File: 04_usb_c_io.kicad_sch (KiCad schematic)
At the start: 38 parts, among them J11 USB-C downstream 1, J12 USB-C downstream 2, U21 TPS25810 Type-C DFP port 1, U22 HD3SS6126 USB3 orientation mu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, U23 TPD4EUSB30 TX ESD, U24 TPD4EUSB30 RX ESD, U25 TPD4EUSB30 USB2/CC ESD, U31 TPS25810 Type-C DFP port 2, U32 HD3SS6126 USB3 orientation mu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, U33 TPD4EUSB30 TX ESD, U34 TPD4EUSB30 RX ESD, U35 TPD4EUSB30 USB2/CC ESD

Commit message: Publish the current Ducktop2 design
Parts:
- removed C70: 10u TPS25810 IN, Capacitor_SMD:C_1206_3216Metric, symbol Device:C
- removed C71: 100n TPS25810 IN, Capacitor_SMD:C_0603_1608Metric, symbol Device:C
- removed C72: 100n AUX, Capacitor_SMD:C_0603_1608Metric, symbol Device:C
- removed C73: 100n mux VDD, Capacitor_SMD:C_0603_1608Metric, symbol Device:C
- removed R92: 10k UFP pull-up, Resistor_SMD:R_0603_1608Metric, symbol Device:R
- removed R93: 10k LD_DET pull-up, Resistor_SMD:R_0603_1608Metric, symbol Device:R
- removed R94: 100k REF, Resistor_SMD:R_0603_1608Metric, symbol Device:R
- removed U24: TPD4EUSB30 RX ESD, Package_SON:USON-10_2.5x1.0mm_P0.5mm, symbol Power_Protection:TPD4EUSB30
- removed U33: TPD4EUSB30 TX ESD, Package_SON:USON-10_2.5x1.0mm_P0.5mm, symbol Power_Protection:TPD4EUSB30
- added C98: 150u 10V TPS25810 input reservoir, Capacitor_Tantalum_SMD:CP_EIA-7343-31_Kemet-D, symbol Device:C_Polarized
- added C99: 10n mux high-frequency bypass, Capacitor_SMD:C_0603_1608Metric, symbol Device:C
- added D210, D211, D212, D213, D214, D215, D216, D217, D230, D231, D232, D233, D234, D235, D236, D237: TPD1E0B04DPL USB3 ESD, Diode_SMD:D_0201_0603Metric, symbol Device:D_TVS
- added R70: 20.0k 1% TPS2553 ILIM 1.3A nominal, Resistor_SMD:R_0603_1608Metric, symbol Device:R
- added R71: 4.99k 1% POL pull-up, Resistor_SMD:R_0603_1608Metric, symbol Device:R
- added R74: 100k 1% <=100ppm REF, Resistor_SMD:R_0603_1608Metric, symbol Device:R
- added U20: TPS2553DDBVR USB-C port 1 1.3A branch switch, Package_TO_SOT_SMD:SOT-23-6, symbol TPS2553D:TPS2553D
- added U30: TPS2553DDBVR USB-C port 2 1.3A branch switch, Package_TO_SOT_SMD:SOT-23-6, symbol TPS2553D:TPS2553D
- C70: renamed from C74; value 100n mux VDD -> 100n TPS2553 input bypass
- C71: renamed from C75; value 10u port VBUS -> 100n TPS25810 IN; footprint Capacitor_SMD:C_1206_3216Metric -> Capacitor_SMD:C_0603_1608Metric
- C72: renamed from C76; value 100n USB3 TX AC -> 100n AUX
- C73: renamed from C77; value 100n USB3 TX AC -> 100n mux VDD
- C74: renamed from R70; value 10k FAULT pull-up -> 100n mux VDD; footprint Resistor_SMD:R_0603_1608Metric -> Capacitor_SMD:C_0603_1608Metric; symbol Device:R -> Device:C
- C75: renamed from R74; value 100k REF -> 10u port VBUS; footprint Resistor_SMD:R_0603_1608Metric -> Capacitor_SMD:C_1206_3216Metric; symbol Device:R -> Device:C
- C76: renamed from R71; value 10k POL pull-up -> 100n mux VDD (third supply pin); footprint Resistor_SMD:R_0603_1608Metric -> Capacitor_SMD:C_0603_1608Metric; symbol Device:R -> Device:C
- C77: renamed from R72; value 10k UFP pull-up -> 1u mux shared bulk; footprint Resistor_SMD:R_0603_1608Metric -> Capacitor_SMD:C_0805_2012Metric; symbol Device:R -> Device:C
- C78: renamed from U23; value TPD4EUSB30 TX ESD -> 150u 10V TPS25810 input reservoir; footprint Package_SON:USON-10_2.5x1.0mm_P0.5mm -> Capacitor_Tantalum_SMD:CP_EIA-7343-31_Kemet-D; symbol Power_Protection:TPD4EUSB30 -> Device:C_Polarized; MPN (none) -> T520D157M010ATE025; Manufacturer (none) -> KEMET
- C79: renamed from R73; value 10k LD_DET pull-up -> 10n mux high-frequency bypass; footprint Resistor_SMD:R_0603_1608Metric -> Capacitor_SMD:C_0603_1608Metric; symbol Device:R -> Device:C
- C90: value 10u TPS25810 IN -> 100n TPS2553 input bypass; footprint Capacitor_SMD:C_1206_3216Metric -> Capacitor_SMD:C_0603_1608Metric
- C96: value 100n USB3 TX AC -> 100n mux VDD (third supply pin)
- C97: value 100n USB3 TX AC -> 1u mux shared bulk; footprint Capacitor_SMD:C_0603_1608Metric -> Capacitor_SMD:C_0805_2012Metric
- J11, J12: MPN (none) -> 105450-0101; Manufacturer (none) -> Molex
- R90: value 10k FAULT pull-up -> 20.0k 1% TPS2553 ILIM 1.3A nominal; MPN (none) -> RC0603FR-0720KL; Manufacturer (none) -> Yageo
- R91: value 10k POL pull-up -> 4.99k 1% POL pull-up
- R94: renamed from U34; value TPD4EUSB30 RX ESD -> 100k 1% <=100ppm REF; footprint Package_SON:USON-10_2.5x1.0mm_P0.5mm -> Resistor_SMD:R_0603_1608Metric; symbol Power_Protection:TPD4EUSB30 -> Device:R
- U21, U31: MPN (none) -> TPS25810RVCR; Manufacturer (none) -> Texas Instruments
- U22, U32: MPN (none) -> HD3SS6126RUAR; Manufacturer (none) -> Texas Instruments
- U25, U35: value TPD4EUSB30 USB2/CC ESD -> TPD4E05U06 USB2/CC ESD; MPN (none) -> TPD4E05U06DQAR; Manufacturer (none) -> Texas Instruments
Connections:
- net HUB1_SSTX_N is gone; now on net SYS_3V3: C73.1
- net HUB1_SSTX_P is gone; now on net SYS_3V3: C72.1
- net HUB2_PE is gone; now on net MU_HOST_ACTIVE: U31.6 (EN)
- net HUB2_SSTX_N is gone; now on net SYS_3V3: C97.1
- net HUB2_SSTX_P is gone; now on net SYS_3V3: C96.1
- net GND: now also C72.2, C73.2, C74.2, C76.2, C77.2, C78.2, C79.2, C96.2, C97.2, R90.2, C98.2, C99.2, D210.2 (A2), D211.2 (A2), D212.2 (A2), D213.2 (A2), D214.2 (A2), D215.2 (A2), D216.2 (A2), D217.2 (A2), D230.2 (A2), D231.2 (A2), D232.2 (A2), D233.2 (A2), D234.2 (A2), D235.2 (A2), D236.2 (A2), D237.2 (A2), R70.2, U20.2 (GND), U30.2 (GND); no longer C78.3 (GND), C78.8 (GND), R94.3 (GND), R94.8 (GND), U21.9 (REF_RTN), U22.6 (HS_~{OE}), U31.9 (REF_RTN), U32.6 (HS_~{OE})
- net SYS_3V3: now also U22.6 (HS_~{OE}), U32.6 (HS_~{OE}), C99.1, R71.1; no longer C70.1, R90.1
- net SYS_5V: now also C70.1, U20.1 (IN), U30.1 (IN); no longer C91.1, U21.2 (IN1), U21.3 (IN1), U21.4 (IN2), U31.2 (IN1), U31.3 (IN1), U31.4 (IN2)
- net USB1_POL_N: now also R71.2; no longer C76.2
- net USB1_REF: now also R74.1; no longer C75.1
- net USB1_RX1_N_CONN: now also U22.22 (SSC1(n)), D215.1 (A1); no longer U22.24 (SSC0(n))
- net USB1_RX1_P_CONN: now also U22.23 (SSC1(p)), D214.1 (A1); no longer U22.25 (SSC0(p))
- net USB1_RX2_N_CONN: now also U22.26 (SSB1(n)), D217.1 (A1); no longer U22.22 (SSC1(n))
- net USB1_RX2_P_CONN: now also U22.27 (SSB1(p)), D216.1 (A1); no longer U22.23 (SSC1(p))
- net USB1_TX1_N_CONN: now also U22.24 (SSC0(n)), D211.1 (A1); no longer C78.2 (D1-), U22.28 (SSB0(n))
- net USB1_TX1_P_CONN: now also U22.25 (SSC0(p)), D210.1 (A1); no longer C78.1 (D1+), U22.29 (SSB0(p))
- net USB1_TX2_N_CONN: now also U22.28 (SSB0(n)), D213.1 (A1); no longer C78.5 (D2-), U22.26 (SSB1(n))
- net USB1_TX2_P_CONN: now also U22.29 (SSB0(p)), D212.1 (A1); no longer C78.4 (D2+), U22.27 (SSB1(p))
- net USB1_VBUS: now also C75.1; no longer C71.1
- net USB2_REF: now also R94.1
- net USB2_RX1_N_CONN: now also U32.22 (SSC1(n)), D235.1 (A1); no longer R94.2 (D1-), U32.24 (SSC0(n))
- net USB2_RX1_P_CONN: now also U32.23 (SSC1(p)), D234.1 (A1); no longer R94.1 (D1+), U32.25 (SSC0(p))
- net USB2_RX2_N_CONN: now also U32.26 (SSB1(n)), D237.1 (A1); no longer R94.5 (D2-), U32.22 (SSC1(n))
- net USB2_RX2_P_CONN: now also U32.27 (SSB1(p)), D236.1 (A1); no longer R94.4 (D2+), U32.23 (SSC1(p))
- net USB2_TX1_N_CONN: now also U32.24 (SSC0(n)), D231.1 (A1); no longer U32.28 (SSB0(n))
- net USB2_TX1_P_CONN: now also U32.25 (SSC0(p)), D230.1 (A1); no longer U32.29 (SSB0(p))
- net USB2_TX2_N_CONN: now also U32.28 (SSB0(n)), D233.1 (A1); no longer U32.26 (SSB1(n))
- net USB2_TX2_P_CONN: now also U32.29 (SSB0(p)), D232.1 (A1); no longer U32.27 (SSB1(p))
- net USBC2_SSTX_P: now reaches U32.11 (SSA0(p))
- net USBC2_SSTX_N: now reaches U32.12 (SSA0(n))
- net USBC2_SSRX_P: now reaches U32.15 (SSA1(p))
- net USBC2_SSRX_N: now reaches U32.16 (SSA1(n))
- net USBC1_SSTX_P: now reaches U22.11 (SSA0(p))
- net USBC1_SSTX_N: now reaches U22.12 (SSA0(n))
- net USBC1_SSRX_P: now reaches U22.15 (SSA1(p))
- net USBC1_SSRX_N: now reaches U22.16 (SSA1(n))
- net HUB1_DM renamed USBC1_DM
- net HUB1_DP renamed USBC1_DP
- net HUB1_OC_N renamed MU_USB_OC_N
- net MU_USB_OC_N: now also U31.1 (~{FAULT}), U20.4 (~{FAULT}), U30.4 (~{FAULT}); no longer C74.2
- net HUB1_PE renamed MU_HOST_ACTIVE
- net MU_HOST_ACTIVE: now also U20.3 (EN), U30.3 (EN)
- net HUB1_SSRX_N: no longer names the net of U22.34 (HSC(n))
- net HUB1_SSRX_P: no longer names the net of U22.33 (HSC(p))
- net HUB2_DM renamed USBC2_DM
- net HUB2_DP renamed USBC2_DP
- removed net HUB2_OC_N: R90.2, U31.1 (~{FAULT})
- net HUB2_SSRX_N: no longer names the net of U32.34 (HSC(n))
- net HUB2_SSRX_P: no longer names the net of U32.33 (HSC(p))
- net USB1_LD_DET_N: no longer names the net of U21.20 (~{LD_DET})
- net USB1_LD_DET_N: no longer C79.2
- net USB1_TX_CAP_N: no longer names the net of U22.32 (HSB(n))
- net USB1_TX_CAP_N: no longer C73.2
- net USB1_TX_CAP_P: no longer names the net of U22.31 (HSB(p))
- net USB1_TX_CAP_P: no longer C72.2
- net USB1_UFP_N: no longer names the net of U21.19 (~{UFP})
- net USB1_UFP_N: no longer C77.2
- net USB2_LD_DET_N: no longer names the net of U31.20 (~{LD_DET})
- net USB2_TX_CAP_N: no longer names the net of U32.32 (HSB(n))
- net USB2_TX_CAP_N: no longer C97.2
- net USB2_TX_CAP_P: no longer names the net of U32.31 (HSB(p))
- net USB2_TX_CAP_P: no longer C96.2
- net USB2_UFP_N: no longer names the net of U31.19 (~{UFP})
- new net USB1_5V_PRE: C71.1, C78.1, U20.6 (OUT), U21.2 (IN1), U21.3 (IN1), U21.4 (IN2)
- new net USB1_ILIM: R70.1, U20.5 (ILIM)
- new net USB1_REF_RTN: R74.2, U21.9 (REF_RTN)
- new net USB2_5V_PRE: C91.1, C98.1, U30.6 (OUT), U31.2 (IN1), U31.3 (IN1), U31.4 (IN2)
- new net USB2_ILIM: R90.1, U30.5 (ILIM)
- new net USB2_REF_RTN: R94.2, U31.9 (REF_RTN)
- no-connect marks 72 -> 60
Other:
- note added: "== J11 native Mu USB 3.2 Gen 2 Type-C host port 1 =="
- note added: "== J12 native Mu USB 3.2 Gen 2 Type-C host port 2 =="
- note added: "== Two native Mu USB 3.2 Gen 2 Type-C host ports =="
- note added: "Both ports use MU_HOST_ACTIVE = PSON AND MU_12V_PG; suspend or a failed Mu rail removes VBUS."
- note added: "CHG/CHG_HI are strapped low for default USB current; branch-switch and port FAULT outputs share Mu USB_OC#."
- note added: "J11: native USB 10Gbps host, default-current advertisement; TCP0 is HDMI-A on sheet 6."
- note added: "J12: native USB 10Gbps host, default-current advertisement; TCP0 is HDMI-A on sheet 6."
- note added: "SYS_5V BUDGET HOLD: default-current ports still share one rail with trackpad, fan, audio, radios, and maker power; simultaneous-load validation/load shedding is mandatory."
- note added: "TPS25810 handles DFP CC/VBUS; TI rates the HD3SS6126 high-bandwidth path up to 10Gbps."
- note removed: "== J11 USB-C downstream port 1 from VL822 =="
- note removed: "== J12 USB-C downstream port 2 from VL822 =="
- note removed: "== USB-C hub I/O: VL822 downstream ports only =="
- note removed: "CHG/CHG_HI are strapped low for standard USB current advertisement."
- note removed: "J11: advertises standard USB current; TCP0 is now the external HDMI-A output on sheet 6."
- note removed: "J12: advertises standard USB current; TCP0 is now the external HDMI-A output on sheet 6."
- note removed: "TPS25810 handles DFP CC/VBUS; HD3SS6126 handles reversible SuperSpeed orientation."
- moved on the sheet: C70, C71, C72, C73

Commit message: Finish USB-C policy and split out radio board
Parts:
- removed C70, C90: 100n TPS2553 input bypass, Capacitor_SMD:C_0603_1608Metric, symbol Device:C
- removed C71, C91: 100n TPS25810 IN, Capacitor_SMD:C_0603_1608Metric, symbol Device:C
- removed C72, C92: 100n AUX, Capacitor_SMD:C_0603_1608Metric, symbol Device:C
- removed C73, C74, C93, C94: 100n mux VDD, Capacitor_SMD:C_0603_1608Metric, symbol Device:C
- removed C75, C95: 10u port VBUS, Capacitor_SMD:C_1206_3216Metric, symbol Device:C
- removed C76, C96: 100n mux VDD (third supply pin), Capacitor_SMD:C_0603_1608Metric, symbol Device:C
- removed C77, C97: 1u mux shared bulk, Capacitor_SMD:C_0805_2012Metric, symbol Device:C
- removed C78, C98: 150u 10V TPS25810 input reservoir, Capacitor_Tantalum_SMD:CP_EIA-7343-31_Kemet-D, symbol Device:C_Polarized
- removed C79, C99: 10n mux high-frequency bypass, Capacitor_SMD:C_0603_1608Metric, symbol Device:C
- removed D211, D212, D213, D214, D215, D216, D217, D230, D231, D232, D233, D234, D235, D236, D237: TPD1E0B04DPL USB3 ESD, Diode_SMD:D_0201_0603Metric, symbol Device:D_TVS
- removed J11: USB-C downstream 1, Connector_USB:USB_C_Receptacle_Molex_105450-0101, symbol Connector:USB_C_Receptacle
- removed R70, R90: 20.0k 1% TPS2553 ILIM 1.3A nominal, Resistor_SMD:R_0603_1608Metric, symbol Device:R
- removed R71, R91: 4.99k 1% POL pull-up, Resistor_SMD:R_0603_1608Metric, symbol Device:R
- removed R94: 100k 1% <=100ppm REF, Resistor_SMD:R_0603_1608Metric, symbol Device:R
- removed U21: TPS25810 Type-C DFP port 1, Package_DFN_QFN:Texas_RVC0020A_WQFN-20-1EP_3x4mm_P0.5mm_EP1.6x2.6mm, symbol Interface_USB:TPS25810RVC
- removed U25, U35: TPD4E05U06 USB2/CC ESD, Package_SON:USON-10_2.5x1.0mm_P0.5mm, symbol Power_Protection:TPD4EUSB30
- removed U30: TPS2553DDBVR USB-C port 2 1.3A branch switch, Package_TO_SOT_SMD:SOT-23-6, symbol TPS2553D:TPS2553D
- removed U31: TPS25810 Type-C DFP port 2, Package_DFN_QFN:Texas_RVC0020A_WQFN-20-1EP_3x4mm_P0.5mm_EP1.6x2.6mm, symbol Interface_USB:TPS25810RVC
- removed U32: HD3SS6126 USB3 orientation mux 2, Package_DFN_QFN:WQFN-42-1EP_3.5x9mm_P0.5mm_EP2.05x7.55mm_ThermalVias, symbol Interface_USB:HD3SS6126
- added C1705: 120p core feed-forward, Capacitor_SMD:C_0402_1005Metric, symbol Device:C
- added C1706: 4.7u core input, Capacitor_SMD:C_0805_2012Metric, symbol Device:C
- added C1707: 100n core input HF, Capacitor_SMD:C_0603_1608Metric, symbol Device:C
- added C1708, C1709: 10u core output, Capacitor_SMD:C_0805_2012Metric, symbol Device:C
- added C1710: 100n USB5 bootstrap, Capacitor_SMD:C_0603_1608Metric, symbol Device:C
- added C1711: 10u 50V USB5 input, Capacitor_SMD:C_1206_3216Metric, symbol Device:C
- added C1713: 100n 50V USB5 input HF, Capacitor_SMD:C_0603_1608Metric, symbol Device:C
- added C1714, C1715: 22u 10V USB5 output, Capacitor_SMD:C_1210_3225Metric, symbol Device:C
- added C1716: 100n oscillator bypass, Capacitor_SMD:C_0603_1608Metric, symbol Device:C
- added C1717: 100n hub reset-gate bypass, Capacitor_SMD:C_0603_1608Metric, symbol Device:C
- added C1720, C1721, C1722, C1723, C1724, C1725, C1726, C1727, C1728, C1729: 100n USB 3.2 TX AC coupling, Capacitor_SMD:C_0402_1005Metric, symbol Device:C
- added C1740, C1760, C1780: 100n branch input, Capacitor_SMD:C_0603_1608Metric, symbol Device:C
- added C1741, C1761, C1781: 100n TPS25810 IN HF, Capacitor_SMD:C_0603_1608Metric, symbol Device:C
- added C1742, C1762, C1782: 150u 10V TPS25810 input reservoir, Capacitor_Tantalum_SMD:CP_EIA-7343-31_Kemet-D, symbol Device:C_Polarized
- added C1743, C1763, C1783: 10u protected VBUS_SYS, Capacitor_SMD:C_1206_3216Metric, symbol Device:C
- added C1744, C1764, C1784: 100n TPS25810 AUX, Capacitor_SMD:C_0603_1608Metric, symbol Device:C
- added C1745, C1746, C1747, C1765, C1766, C1767, C1785, C1786, C1787: 100n mux VDD, Capacitor_SMD:C_0603_1608Metric, symbol Device:C
- added C1748, C1768, C1788: 1u mux local bulk, Capacitor_SMD:C_0603_1608Metric, symbol Device:C
- added C1749, C1769, C1789: 10n mux HF, Capacitor_SMD:C_0402_1005Metric, symbol Device:C
- added C1750, C1770, C1790: 1u 50V connector-side VBUS, Capacitor_SMD:C_0805_2012Metric, symbol Device:C
- added C1751, C1771, C1791: 1u TPD1S514 VBUS_POWER stability, Capacitor_SMD:C_0603_1608Metric, symbol Device:C
- added C1810, C1811, C1812, C1813, C1814, C1815, C1816, C1817: 100n USB7206C VDD33 local, Capacitor_SMD:C_0603_1608Metric, symbol Device:C
- added C1820, C1821, C1822, C1823, C1824, C1825, C1826, C1827, C1828: 100n USB7206C VCORE local, Capacitor_SMD:C_0603_1608Metric, symbol Device:C
- added C1830, C1831, C1832, C1833, C1834, C1835, C1836, C1837: 1n USB7206C VDD33 HF, Capacitor_SMD:C_0402_1005Metric, symbol Device:C
- added C1840, C1841, C1842, C1843, C1844, C1845, C1846, C1847, C1848: 1n USB7206C VCORE HF, Capacitor_SMD:C_0402_1005Metric, symbol Device:C
- added C1849: 10u USB7206C VDD33 bulk, Capacitor_SMD:C_0805_2012Metric, symbol Device:C
- added D1800, D1801, D1802, D1803, D1804, D1805, D1806, D1807, D1808, D1809, D1810, D1811, D1812, D1813, D1814, D1815, D1816, D1817, D1818, D1819, D1820, D1821, D1822, D1823: TPD1E0B04DPLR 0.13pF USB3 ESD, Diode_SMD:D_0201_0603Metric, symbol TPD1E0B04:TPD1E0B04
- added J22: USB-C source-only data port J22, Connector_USB:USB_C_Receptacle_Molex_105450-0101, symbol Connector:USB_C_Receptacle
- added J23: USB-C source-only data port J23, Connector_USB:USB_C_Receptacle_Molex_105450-0101, symbol Connector:USB_C_Receptacle
- added L1700: 470nH >=3.9A USB hub core, ducktop2:TDK_TFM201610, symbol Device:L
- added L1701: 3.3uH >=9A USB port buck, Inductor_SMD:L_Coilcraft_XAL7070-XXX, symbol Device:L
- added R1700: 10k CFG_STRAP1, Resistor_SMD:R_0603_1608Metric, symbol Device:R
- added R1701: 200k CFG_STRAP2, Resistor_SMD:R_0603_1608Metric, symbol Device:R
- added R1702: 200k CFG_STRAP3, Resistor_SMD:R_0603_1608Metric, symbol Device:R
- added R1703: 200k all ports removable, Resistor_SMD:R_0603_1608Metric, symbol Device:R
- added R1704: 200k BC1.2 disabled, Resistor_SMD:R_0603_1608Metric, symbol Device:R
- added R1705: 91.0k 1% core FB top, Resistor_SMD:R_0603_1608Metric, symbol Device:R
- added R1706: 100k 1% core FB bottom, Resistor_SMD:R_0603_1608Metric, symbol Device:R
- added R1707: 100k core PG pull-up, Resistor_SMD:R_0603_1608Metric, symbol Device:R
- added R1708: 12.0k 1% USB7206C RBIAS, Resistor_SMD:R_0603_1608Metric, symbol Device:R
- added R1710: 169k 1% USB5 EN top, Resistor_SMD:R_0603_1608Metric, symbol Device:R
- added R1711: 36.1k 1% USB5 EN bottom, Resistor_SMD:R_0603_1608Metric, symbol Device:R
- added R1712: 76.8k 1% USB5 FB top, Resistor_SMD:R_0603_1608Metric, symbol Device:R
- added R1713: 10.0k 1% USB5 FB bottom, Resistor_SMD:R_0603_1608Metric, symbol Device:R
- added R1714: 100k USB5 PG pull-up, Resistor_SMD:R_0603_1608Metric, symbol Device:R
- added R1715, R1716, R1717: 10k TEST pull-up, Resistor_SMD:R_0603_1608Metric, symbol Device:R
- added R1718: 10k hub 3V3 supervisor pull-up, Resistor_SMD:R_0603_1608Metric, symbol Device:R
- added R1720, R1721, R1722, R1723: 100k unused SPI pull-down, Resistor_SMD:R_0603_1608Metric, symbol Device:R
- added R1730, R1731, R1732, R1733: 0R unused-port disable strap to 3V3, Resistor_SMD:R_0603_1608Metric, symbol Device:R
- added R1740, R1760, R1780: 20.0k 1% TPS2553 1.3A ILIM, Resistor_SMD:R_0603_1608Metric, symbol Device:R
- added R1741, R1761, R1781: 4.99k POL pull-up, Resistor_SMD:R_0603_1608Metric, symbol Device:R
- added R1742, R1762, R1782: 100k 1% TPS25810 REF, Resistor_SMD:R_0603_1608Metric, symbol Device:R
- added R1750, R1770, R1790: 249R 0.25W TPS25810 OUT discharge, Resistor_SMD:R_1206_3216Metric, symbol Device:R
- added unit 4 of U1700
- added unit 1 of U1700
- added unit 5 of U1700
- added unit 3 of U1700
- added U1701: TPS62823DLC 3A USB7206C 1.146V core buck, Package_SON:Texas_VSON-HR-8_1.5x2mm_P0.5mm, symbol Regulator_Switching:TPS62823DLC
- added U1702: TLV803EA29 USB hub reset supervisor, Package_TO_SOT_SMD:SOT-23-3, symbol TLV803EA29RDBZR:TLV803EA29RDBZR
- added U1704: SN74LVC1G08 hub 3V3/core-PG reset gate, Package_TO_SOT_SMD:SOT-23-5, symbol 74xGxx:74LVC1G08
- added U1740, U1760, U1780: TPS2553DDBVR 1.3A USB branch, Package_TO_SOT_SMD:SOT-23-6, symbol TPS2553D:TPS2553D
- added U1741, U1761, U1781: TPS25810RVCR Type-C DFP controller, Package_DFN_QFN:Texas_RVC0020A_WQFN-20-1EP_3x4mm_P0.5mm_EP1.6x2.6mm, symbol Interface_USB:TPS25810RVC
- added U1742, U1762, U1782: HD3SS6126RUAR USB3 orientation mux, Package_DFN_QFN:WQFN-42-1EP_3.5x9mm_P0.5mm_EP2.05x7.55mm_ThermalVias, symbol Interface_USB:HD3SS6126
- added U1743, U1763, U1783: TPD1S514-1YZR 5.9V VBUS OVP, ducktop2:Texas_TPD1S514_YZ_WCSP-12_1.99x1.29mm_P0.5mm, symbol TPD1S514_1YZR:TPD1S514_1YZR
- added U1745, U1765, U1785: TPD4E05U06 USB2/CC ESD, Package_SON:USON-10_2.5x1.0mm_P0.5mm, symbol Power_Protection:TPD4E05U06DQA
- added Y1700: 25.000MHz 3.3V USB hub oscillator, Oscillator:Oscillator_SMD_Abracon_ASDMB-4Pin_2.5x2.0mm, symbol Oscillator:ASDMB-xxxMHz
- C1712: renamed from U22; value HD3SS6126 USB3 orientation mux 1 -> 10u 50V USB5 input; footprint Package_DFN_QFN:WQFN-42-1EP_3.5x9mm_P0.5mm_EP2.05x7.55mm_ThermalVias -> Capacitor_SMD:C_1206_3216Metric; symbol Interface_USB:HD3SS6126 -> Device:C; MPN HD3SS6126RUAR -> CGA5L1X7R1H106K160AC; Manufacturer Texas Instruments -> Murata
- J12: value USB-C downstream 2 -> USB-C source-only data port J12
- R1840: renamed from R74; value 100k 1% <=100ppm REF -> 10k DS1 PRT_CTL idle pull-up; VBUS is managed by its TCPC; MPN (none) -> RC0603FR-0710KL; Manufacturer (none) -> Yageo
- U1700: renamed from D210; value TPD1E0B04DPL USB3 ESD -> USB7206C-I/KDX six-port USB 3.2 Gen 2 hub; footprint Diode_SMD:D_0201_0603Metric -> Package_DFN_QFN:VQFN-100-1EP_12x12mm_P0.4mm_EP8x8mm_ThermalVias; symbol Device:D_TVS -> USB7206C:USB7206C; MPN TPD1E0B04DPLR -> USB7206C-I/KDX; Manufacturer Texas Instruments -> Microchip
- U1703: renamed from U20; value TPS2553DDBVR USB-C port 1 1.3A branch switch -> TPS56637RPAR VSYS to USB_PORT_5V 5.21V; footprint Package_TO_SOT_SMD:SOT-23-6 -> ducktop2:Texas_RPA0010A_VQFN-HR-10_3x3mm; symbol TPS2553D:TPS2553D -> TPS56637:TPS56637; MPN TPS2553DDBVR -> TPS56637RPAR
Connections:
- net MU_HOST_ACTIVE is gone; now on net GND: U1703.3 (AGND)
- net USB1_REF is gone; now on net SYS_3V3: R1840.1
- net GND: now also C1712.2, U1703.10 (MODE), U1703.9 (PGND), C1706.2, C1707.2, C1708.2, C1709.2, C1711.2, C1713.2, C1714.2, C1715.2, C1716.2, C1717.2, C1740.2, C1741.2, C1742.2, C1743.2, C1744.2, C1745.2, C1746.2, C1747.2, C1748.2, C1749.2, C1750.2, C1751.2, C1760.2, C1761.2, C1762.2, C1763.2, C1764.2, C1765.2, C1766.2, C1767.2, C1768.2, C1769.2, C1770.2, C1771.2, C1780.2, C1781.2, C1782.2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; no longer C1712.10 (GND), C1712.14 (GND), C1712.17 (GND), C1712.19 (GND), C1712.21 (GND), C1712.43 (EPAD), U1700.2 (A2), U1703.2 (GND)
- net SYS_3V3: now also C1706.1, C1707.1, C1716.1, C1717.1, C1744.1, C1745.1, C1746.1, C1747.1, C1748.1, C1749.1, C1764.1, C1765.1, C1766.1, C1767.1, C1768.1, C1769.1, C1784.1, C1785.1, C1786.1, C1787.1, C1788.1, C1789.1, C1810.1, C1811.1, C1812.1, C1813.1, C1814.1, C1815.1, C1816.1, C1817.1, C1830.1, C1831.1, C1832.1, C1833.1, C1834.1, C1835.1, C1836.1, C1837.1, C1849.1, R1707.1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; no longer C1712.13 (VDD), C1712.20 (VDD), C1712.30 (VDD), C1712.6 (HS_~{OE})
- net USBC2_DM: now also U1700.90 (USB2UP_DM); no longer J12.A7 (D-), J12.B7 (D-)
- net USBC2_DP: now also U1700.89 (USB2UP_DP); no longer J12.A6 (D+), J12.B6 (D+)
- net USBC2_SSRX_N: now also C1729.2
- net USBC2_SSRX_P: now also C1728.2
- net USBC2_SSTX_N: now also U1700.95 (USB3UP_RXDM)
- net USBC2_SSTX_P: now also U1700.94 (USB3UP_RXDP)
- net VSYS: now reaches C1712.1
- net VSYS: now also U1703.8 (VIN), C1711.1, C1713.1, R1710.1
- net MU_USB_OC_N renamed USB5_PG
- net USB5_PG: now also R1714.2
- net SYS_5V renamed USB5_EN
- net USB5_EN: now also R1710.2, R1711.1
- net USB1_5V_PRE renamed USB5_SW
- net USB5_SW: now also C1710.2, L1701.1
- net USB1_ILIM: no longer names the net of U1703.5 (NC)
- removed net USB1_POL_N: C1712.9 (SEL)
- net USB1_REF_RTN renamed HUB_DS1_PRT_CTL
- net HUB_DS1_PRT_CTL: now also U1700.60 (PF17)
- removed net USB1_RX1_N_CONN: C1712.22 (SSC1(n))
- removed net USB1_RX1_P_CONN: C1712.23 (SSC1(p))
- removed net USB1_RX2_N_CONN: C1712.26 (SSB1(n))
- removed net USB1_RX2_P_CONN: C1712.27 (SSB1(p))
- removed net USB1_TX1_N_CONN: C1712.24 (SSC0(n))
- removed net USB1_TX1_P_CONN: C1712.25 (SSC0(p)), U1700.1 (A1)
- removed net USB1_TX2_N_CONN: C1712.28 (SSB0(n))
- removed net USB1_TX2_P_CONN: C1712.29 (SSB0(p))
- net USB2_CC1 renamed J12_CC1
- net J12_CC1: now also U1761.11 (CC1), U1765.4 (D2+)
- net USB2_CC2 renamed J12_CC2
- net J12_CC2: now also U1761.13 (CC2), U1765.5 (D2-)
- net USB2_RX1_N_CONN renamed J12_RX1_N
- net J12_RX1_N: now also D1821.1 (IO), U1762.22 (SSC1(n))
- net USB2_RX1_P_CONN renamed J12_RX1_P
- net J12_RX1_P: now also D1820.1 (IO), U1762.23 (SSC1(p))
- net USB2_RX2_N_CONN renamed J12_RX2_N
- net J12_RX2_N: now also D1823.1 (IO), U1762.26 (SSB1(n))
- net USB2_RX2_P_CONN renamed J12_RX2_P
- net J12_RX2_P: now also D1822.1 (IO), U1762.27 (SSB1(p))
- net USB2_TX1_N_CONN renamed J12_TX1_N
- net J12_TX1_N: now also D1817.1 (IO), U1762.24 (SSC0(n))
- net USB2_TX1_P_CONN renamed J12_TX1_P
- net J12_TX1_P: now also D1816.1 (IO), U1762.25 (SSC0(p))
- net USB2_TX2_N_CONN renamed J12_TX2_N
- net J12_TX2_N: now also D1819.1 (IO), U1762.28 (SSB0(n))
- net USB2_TX2_P_CONN renamed J12_TX2_P
- net J12_TX2_P: now also D1818.1 (IO), U1762.29 (SSB0(p))
- net USB2_VBUS renamed J12_VBUS
- net J12_VBUS: now also C1770.1, U1763.B3 (VBUS_CON), U1763.C2 (VBUS_CON), U1763.C3 (VBUS_CON)
- removed net USBC1_SSRX_N: C1712.16 (SSA1(n))
- removed net USBC1_SSRX_P: C1712.15 (SSA1(p))
- removed net USBC1_SSTX_N: C1712.12 (SSA0(n))
- removed net USBC1_SSTX_P: C1712.11 (SSA0(p))
- new net HUB_3V3_OK: R1718.2, U1702.1 (RESETz), U1704.1
- new net HUB_BC_EN: R1704.1, U1700.70 (SPI_D0/CFG_BC_EN/PF22)
- new net HUB_CFG1: R1700.1, U1700.21 (CFG_STRAP1)
- new net HUB_CFG2: R1701.1, U1700.22 (CFG_STRAP2)
- new net HUB_CFG3: R1702.1, U1700.23 (CFG_STRAP3)
- new net HUB_CLK: U1700.98 (XTALI/CLK_IN), Y1700.3 (Out)
- new net HUB_CORE_FB: C1705.2, R1705.2, R1706.1, U1701.2 (FB)
- new net HUB_CORE_PG: R1707.2, U1701.8 (PG), U1704.2
- new net HUB_CORE_SW: L1700.1, U1701.6 (SW)
- new net HUB_DIS5_DM: R1731.2, U1700.82 (DM5)
- new net HUB_DIS5_DP: R1730.2, U1700.81 (DP5)
- new net HUB_DIS6_DM: R1733.2, U1700.41 (DM6)
- new net HUB_DIS6_DP: R1732.2, U1700.42 (DP6)
- new net HUB_DS1_DM: U1700.6 (DM1)
- new net HUB_DS1_DP: U1700.5 (DP1)
- new net HUB_DS1_SSRX_N: U1700.11 (RXDM1)
- new net HUB_DS1_SSRX_P: U1700.10 (RXDP1)
- new net HUB_DS1_SSTX_N: C1721.2
- new net HUB_DS1_SSTX_P: C1720.2
- new net HUB_DS1_TX_RAW_N: C1721.1, U1700.8 (TXDM1)
- new net HUB_DS1_TX_RAW_P: C1720.1, U1700.7 (TXDP1)
- new net HUB_DS2_DM: J22.A7 (D-), J22.B7 (D-), U1700.15 (DM2), U1785.2 (D1-)
- new net HUB_DS2_DP: J22.A6 (D+), J22.B6 (D+), U1700.14 (DP2), U1785.1 (D1+)
- new net HUB_DS2_SSRX_N: U1700.20 (RXDM2), U1782.16 (SSA1(n))
- new net HUB_DS2_SSRX_P: U1700.19 (RXDP2), U1782.15 (SSA1(p))
- new net HUB_DS2_SSTX_N: C1723.2, U1782.12 (SSA0(n))
- new net HUB_DS2_SSTX_P: C1722.2, U1782.11 (SSA0(p))
- new net HUB_DS2_TX_RAW_N: C1723.1, U1700.17 (TXDM2)
- new net HUB_DS2_TX_RAW_P: C1722.1, U1700.16 (TXDP2)
- new net HUB_DS3_DM: J23.A7 (D-), J23.B7 (D-), U1700.28 (DM3), U1745.2 (D1-)
- new net HUB_DS3_DP: J23.A6 (D+), J23.B6 (D+), U1700.27 (DP3), U1745.1 (D1+)
- new net HUB_DS3_SSRX_N: U1700.33 (RXDM3), U1742.16 (SSA1(n))
- new net HUB_DS3_SSRX_P: U1700.32 (RXDP3), U1742.15 (SSA1(p))
- new net HUB_DS3_SSTX_N: C1725.2, U1742.12 (SSA0(n))
- new net HUB_DS3_SSTX_P: C1724.2, U1742.11 (SSA0(p))
- new net HUB_DS3_TX_RAW_N: C1725.1, U1700.30 (TXDM3)
- new net HUB_DS3_TX_RAW_P: C1724.1, U1700.29 (TXDP3)
- new net HUB_DS4_DM: J12.A7 (D-), J12.B7 (D-), U1700.35 (DM4), U1765.2 (D1-)
- new net HUB_DS4_DP: J12.A6 (D+), J12.B6 (D+), U1700.34 (DP4), U1765.1 (D1+)
- new net HUB_DS4_SSRX_N: U1700.40 (RXDM4), U1762.16 (SSA1(n))
- new net HUB_DS4_SSRX_P: U1700.39 (RXDP4), U1762.15 (SSA1(p))
- new net HUB_DS4_SSTX_N: C1727.2, U1762.12 (SSA0(n))
- new net HUB_DS4_SSTX_P: C1726.2, U1762.11 (SSA0(p))
- new net HUB_DS4_TX_RAW_N: C1727.1, U1700.37 (TXDM4)
- new net HUB_DS4_TX_RAW_P: C1726.1, U1700.36 (TXDP4)
- new net HUB_NON_REM: R1703.1, U1700.69 (SPI_CE_N/CFG_NON_REM/PF20)
- new net HUB_PRT_CTL2: U1700.59 (PF16), U1780.3 (EN), U1780.4 (~{FAULT}), U1781.1 (~{FAULT}), U1781.6 (EN)
- new net HUB_PRT_CTL3: U1700.58 (PF15), U1740.3 (EN), U1740.4 (~{FAULT}), U1741.1 (~{FAULT}), U1741.6 (EN)
- new net HUB_PRT_CTL4: U1700.57 (PF14), U1760.3 (EN), U1760.4 (~{FAULT}), U1761.1 (~{FAULT}), U1761.6 (EN)
- new net HUB_RBIAS: R1708.1, U1700.100 (RBIAS)
- new net HUB_RESET_N: U1700.1 (RESET_N), U1704.4
- new net HUB_SPI_CLK: R1720.1, U1700.68 (SPI_CLK/PF21)
- new net HUB_SPI_D1: R1721.1, U1700.71 (SPI_D1/PF23)
- new net HUB_SPI_D2: R1722.1, U1700.72 (SPI_D2/PF24)
- new net HUB_SPI_D3: R1723.1, U1700.73 (SPI_D3/PF25)
- new net HUB_TEST1: R1715.2, U1700.63 (TEST1)
- new net HUB_TEST2: R1716.2, U1700.64 (TEST2)
- new net HUB_TEST3: R1717.2, U1700.65 (TEST3)
- new net HUB_UP_TX_RAW_N: C1729.1, U1700.92 (USB3UP_TXDM)
- new net HUB_UP_TX_RAW_P: C1728.1, U1700.91 (USB3UP_TXDP)
- new net HUB_VCORE: C1705.1, C1708.1, C1709.1, C1820.1, C1821.1, C1822.1, C1823.1, C1824.1, C1825.1, C1826.1, C1827.1, C1828.1, C1840.1, C1841.1, C1842.1, C1843.1, C1844.1, C1845.1, C1846.1, C1847.1, C1848.1, L1700.2, R1705.1, U1700.18 (VCORE), U1700.25 (VCORE), U1700.31 (VCORE), U1700.38 (VCORE), U1700.55 (VCORE), U1700.78 (VCORE), U1700.85 (VCORE), U1700.9 (VCORE), U1700.93 (VCORE)
- new net INTERNAL_USB_VBUS_VALID: U1700.2 (PF30/VBUS_DET)
- new net J12_5V_PRE: C1761.1, C1762.1, U1760.6 (OUT), U1761.2 (IN1), U1761.3 (IN1), U1761.4 (IN2)
- new net J12_ILIM: R1760.1, U1760.5 (ILIM)
- new net J12_POL_N: R1761.2, U1761.18 (~{POL}), U1762.9 (SEL)
- new net J12_REF: R1762.1, U1761.10 (REF)
- new net J12_REF_RTN: R1762.2, U1761.9 (REF_RTN)
- new net J12_VBUS_POWER: C1771.1, U1763.B1 (VBUS_POWER)
- new net J12_VBUS_SYS: C1763.1, R1770.1, U1761.14 (OUT), U1761.15 (OUT), U1763.A2 (VBUS_SYS), U1763.A3 (VBUS_SYS), U1763.B2 (VBUS_SYS)
- new net J22_5V_PRE: C1781.1, C1782.1, U1780.6 (OUT), U1781.2 (IN1), U1781.3 (IN1), U1781.4 (IN2)
- new net J22_CC1: J22.A5 (CC1), U1781.11 (CC1), U1785.4 (D2+)
- new net J22_CC2: J22.B5 (CC2), U1781.13 (CC2), U1785.5 (D2-)
- new net J22_ILIM: R1780.1, U1780.5 (ILIM)
- new net J22_POL_N: R1781.2, U1781.18 (~{POL}), U1782.9 (SEL)
- new net J22_REF: R1782.1, U1781.10 (REF)
- new net J22_REF_RTN: R1782.2, U1781.9 (REF_RTN)
- new net J22_RX1_N: D1805.1 (IO), J22.B10 (RX1-), U1782.22 (SSC1(n))
- new net J22_RX1_P: D1804.1 (IO), J22.B11 (RX1+), U1782.23 (SSC1(p))
- new net J22_RX2_N: D1807.1 (IO), J22.A10 (RX2-), U1782.26 (SSB1(n))
- new net J22_RX2_P: D1806.1 (IO), J22.A11 (RX2+), U1782.27 (SSB1(p))
- new net J22_TX1_N: D1801.1 (IO), J22.A3 (TX1-), U1782.24 (SSC0(n))
- new net J22_TX1_P: D1800.1 (IO), J22.A2 (TX1+), U1782.25 (SSC0(p))
- new net J22_TX2_N: D1803.1 (IO), J22.B3 (TX2-), U1782.28 (SSB0(n))
- new net J22_TX2_P: D1802.1 (IO), J22.B2 (TX2+), U1782.29 (SSB0(p))
- new net J22_VBUS: C1790.1, J22.A4 (VBUS), J22.A9 (VBUS), J22.B4 (VBUS), J22.B9 (VBUS), U1783.B3 (VBUS_CON), U1783.C2 (VBUS_CON), U1783.C3 (VBUS_CON)
- new net J22_VBUS_POWER: C1791.1, U1783.B1 (VBUS_POWER)
- new net J22_VBUS_SYS: C1783.1, R1790.1, U1781.14 (OUT), U1781.15 (OUT), U1783.A2 (VBUS_SYS), U1783.A3 (VBUS_SYS), U1783.B2 (VBUS_SYS)
- new net J23_5V_PRE: C1741.1, C1742.1, U1740.6 (OUT), U1741.2 (IN1), U1741.3 (IN1), U1741.4 (IN2)
- new net J23_CC1: J23.A5 (CC1), U1741.11 (CC1), U1745.4 (D2+)
- new net J23_CC2: J23.B5 (CC2), U1741.13 (CC2), U1745.5 (D2-)
- new net J23_ILIM: R1740.1, U1740.5 (ILIM)
- new net J23_POL_N: R1741.2, U1741.18 (~{POL}), U1742.9 (SEL)
- new net J23_REF: R1742.1, U1741.10 (REF)
- new net J23_REF_RTN: R1742.2, U1741.9 (REF_RTN)
- new net J23_RX1_N: D1813.1 (IO), J23.B10 (RX1-), U1742.22 (SSC1(n))
- new net J23_RX1_P: D1812.1 (IO), J23.B11 (RX1+), U1742.23 (SSC1(p))
- new net J23_RX2_N: D1815.1 (IO), J23.A10 (RX2-), U1742.26 (SSB1(n))
- new net J23_RX2_P: D1814.1 (IO), J23.A11 (RX2+), U1742.27 (SSB1(p))
- new net J23_TX1_N: D1809.1 (IO), J23.A3 (TX1-), U1742.24 (SSC0(n))
- new net J23_TX1_P: D1808.1 (IO), J23.A2 (TX1+), U1742.25 (SSC0(p))
- new net J23_TX2_N: D1811.1 (IO), J23.B3 (TX2-), U1742.28 (SSB0(n))
- new net J23_TX2_P: D1810.1 (IO), J23.B2 (TX2+), U1742.29 (SSB0(p))
- new net J23_VBUS: C1750.1, J23.A4 (VBUS), J23.A9 (VBUS), J23.B4 (VBUS), J23.B9 (VBUS), U1743.B3 (VBUS_CON), U1743.C2 (VBUS_CON), U1743.C3 (VBUS_CON)
- new net J23_VBUS_POWER: C1751.1, U1743.B1 (VBUS_POWER)
- new net J23_VBUS_SYS: C1743.1, R1750.1, U1741.14 (OUT), U1741.15 (OUT), U1743.A2 (VBUS_SYS), U1743.A3 (VBUS_SYS), U1743.B2 (VBUS_SYS)
- new net USB5_BOOT: C1710.1, U1703.7 (BOOT)
- new net USB5_FB: R1712.2, R1713.1, U1703.2 (FB)
- new net USB_PORT_5V: C1714.1, C1715.1, C1740.1, C1760.1, C1780.1, L1701.2, R1712.1, U1740.1 (IN), U1760.1 (IN), U1780.1 (IN)
- no-connect marks 60 -> 120
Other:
- note added: "== Dedicated 6A-class port rail and 1.15V hub-core rail =="
- note added: "== Five-port external USB architecture: USB7206C hub and three source-only Type-C ports =="
- note added: "== J12: source-only USB-C data port, USB7206C downstream 4 =="
- note added: "== J22: source-only USB-C data port, USB7206C downstream 2 =="
- note added: "== J23: source-only USB-C data port, USB7206C downstream 3 =="
- note added: "J22, J23, and J12 are data/source-only. TPD1S514-1 blocks forced high-voltage VBUS; compliant charger attach is a safe no-op."
- note added: "Mu HSIO1 plus USB2_P4 is the hub upstream. Hub port 1 feeds rear-right dual-role J11 on sheet 5."
- note added: "USB7206C VBUS_DET follows supervised physical host VBUS; unused ports 5/6 are disabled by DP/DM high straps."
- note added: "USB_PORT_5V is private to the five external ports; per-port current limiting prevents one cable fault from dropping the laptop."
- note removed: "== J11 native Mu USB 3.2 Gen 2 Type-C host port 1 =="
- note removed: "== J12 native Mu USB 3.2 Gen 2 Type-C host port 2 =="
- note removed: "== Two native Mu USB 3.2 Gen 2 Type-C host ports =="
- note removed: "Both ports use MU_HOST_ACTIVE = PSON AND MU_12V_PG; suspend or a failed Mu rail removes VBUS."
- note removed: "CHG/CHG_HI are strapped low for default USB current; branch-switch and port FAULT outputs share Mu USB_OC#."
- note removed: "J11: native USB 10Gbps host, default-current advertisement; TCP0 is HDMI-A on sheet 6."
- note removed: "J12: native USB 10Gbps host, default-current advertisement; TCP0 is HDMI-A on sheet 6."
- note removed: "SYS_5V BUDGET HOLD: default-current ports still share one rail with trackpad, fan, audio, radios, and maker power; simultaneous-load validation/load shedding is mandatory."
- note removed: "TPS25810 handles DFP CC/VBUS; TI rates the HD3SS6126 high-bandwidth path up to 10Gbps."
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
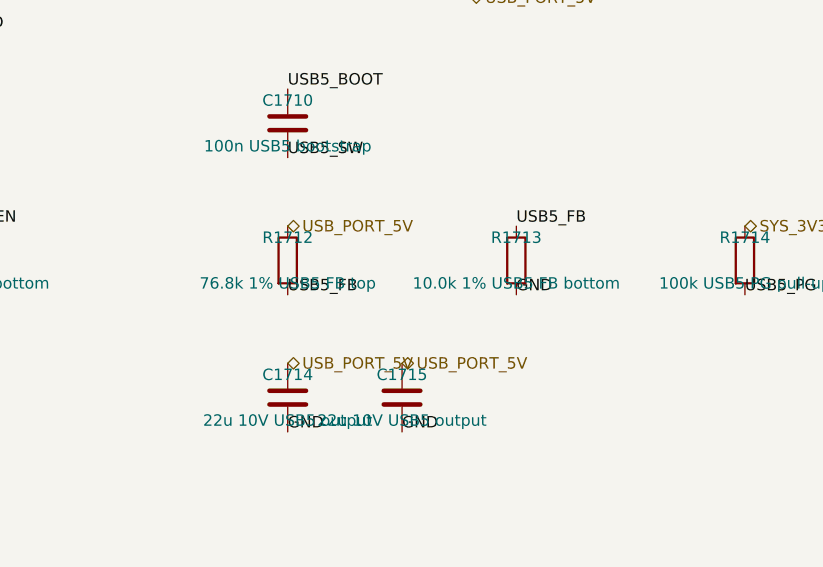
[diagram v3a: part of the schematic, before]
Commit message: Refresh repository with updated PCB renders and current design state
- New 3D renders: top, bottom, perspective, and keyboard PCB
  (generated via kicad-cli 10.0.4, 2560x1440, high quality)
- Update README status: placement complete, coupling caps relocated,
  independent design review CONDITIONAL PASS (2026-07-21)
- Add keyboard rev-A fullboard stencil generation (3MF, STL, manifest, script)
- Track TPS3897ADRYR library symbol
- WIP schematic, PCB, and generator refinements post-coupling-cap fix
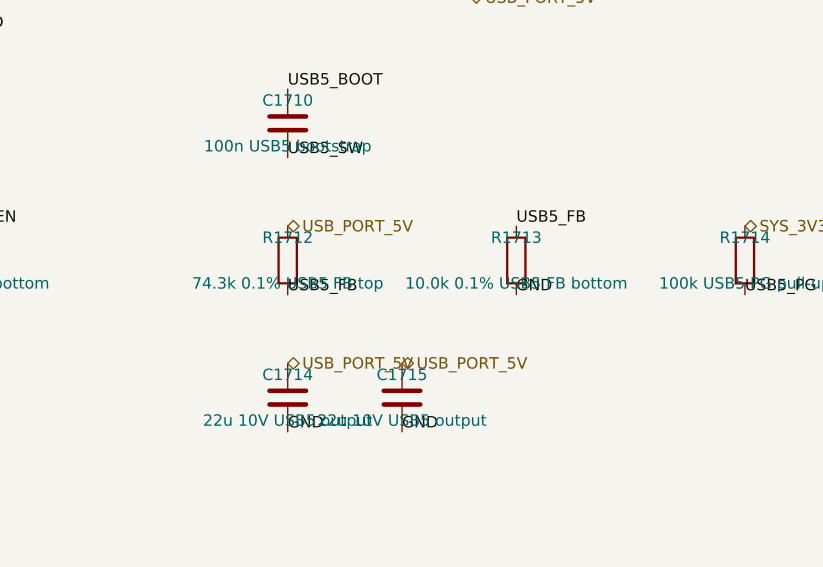
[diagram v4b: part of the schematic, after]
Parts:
- R1712: value 76.8k 1% USB5 FB top -> 74.3k 0.1% USB5 FB top; MPN RC0603FR-0776K8L -> RT0603BRD0743KL
- R1713: value 10.0k 1% USB5 FB bottom -> 10.0k 0.1% USB5 FB bottom; MPN RC0603FR-0710KL -> RT0603BRD0710KL
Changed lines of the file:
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@@
   (dnp no)
   (property "Reference" "R1712" (at 101.6 104.14 0) (effects (font (size 1.27 1.27))))
-  (property "Value" "76.8k 1% USB5 FB top" (at 101.6 109.22 0) (effects (font (size 1.27 1.27))))
+  (property "Value" "74.3k 0.1% USB5 FB top" (at 101.6 109.22 0) (effects (font (size 1.27 1.27))))
   (property "Footprint" "Resistor_SMD:R_0603_1608Metric" (at 101.6 106.68 0) (effects (font (size 1.27 1.27)) (hide yes)))
   (property "Datasheet" "" (at 101.6 106.68 0) (effects (font (size 1.27 1.27)) (hide yes)))
   (property "Manufacturer" "Yageo" (at 101.6 106.68 0) (effects (font (size 1.27 1.27)) (hide yes)))
-  (property "MPN" "RC0603FR-0776K8L" (at 101.6 106.68 0) (effects (font (size 1.27 1.27)) (hide yes)))
+  (property "MPN" "RT0603BRD0743KL" (at 101.6 106.68 0) (effects (font (size 1.27 1.27)) (hide yes)))
   (pin "1")
   (pin "2")
@@
   (dnp no)
   (property "Reference" "R1713" (at 127 104.14 0) (effects (font (size 1.27 1.27))))
-  (property "Value" "10.0k 1% USB5 FB bottom" (at 127 109.22 0) (effects (font (size 1.27 1.27))))
+  (property "Value" "10.0k 0.1% USB5 FB bottom" (at 127 109.22 0) (effects (font (size 1.27 1.27))))
   (property "Footprint" "Resistor_SMD:R_0603_1608Metric" (at 127 106.68 0) (effects (font (size 1.27 1.27)) (hide yes)))
   (property "Datasheet" "" (at 127 106.68 0) (effects (font (size 1.27 1.27)) (hide yes)))
   (property "Manufacturer" "Yageo" (at 127 106.68 0) (effects (font (size 1.27 1.27)) (hide yes)))
-  (property "MPN" "RC0603FR-0710KL" (at 127 106.68 0) (effects (font (size 1.27 1.27)) (hide yes)))
+  (property "MPN" "RT0603BRD0710KL" (at 127 106.68 0) (effects (font (size 1.27 1.27)) (hide yes)))
   (pin "1")
   (pin "2")

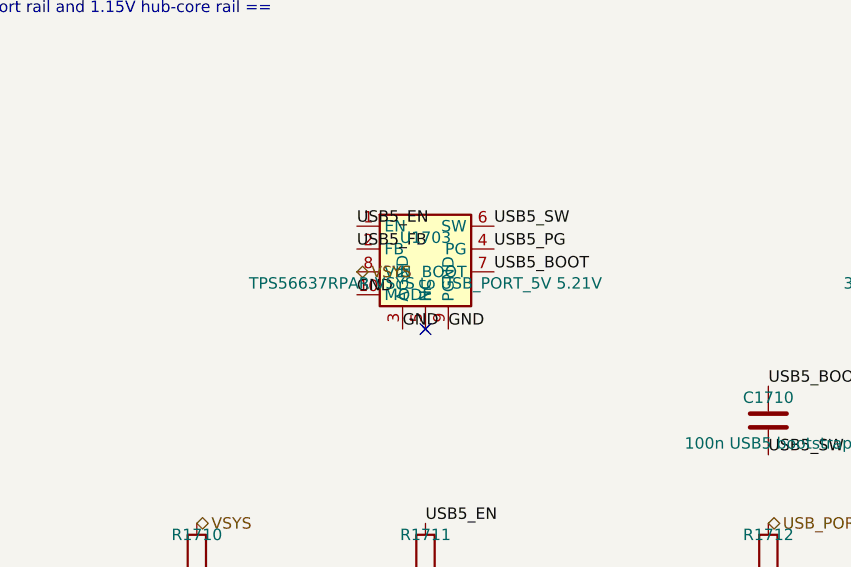
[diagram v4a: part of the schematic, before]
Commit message: Wire the trackpad directly over USB2 and record audit holds
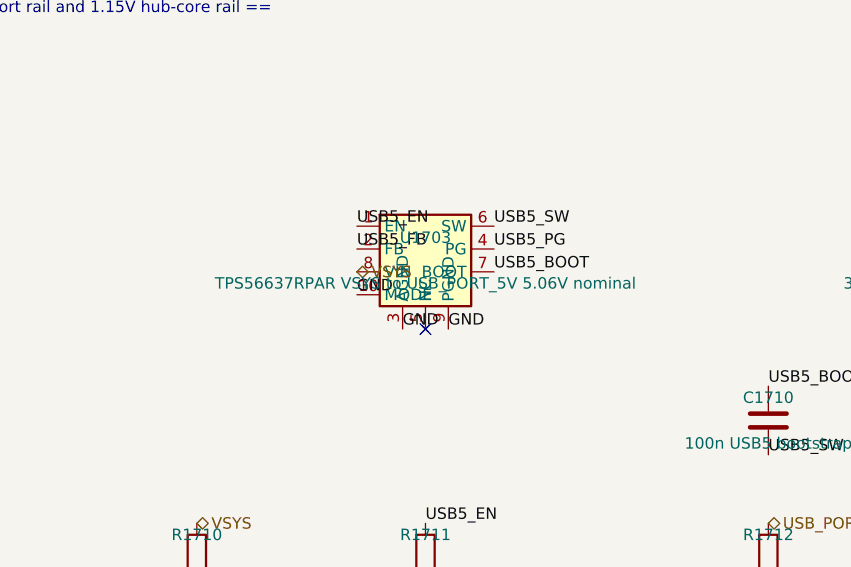
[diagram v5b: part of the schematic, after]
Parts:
- U1703: value TPS56637RPAR VSYS to USB_PORT_5V 5.21V -> TPS56637RPAR VSYS to USB_PORT_5V 5.06V nominal
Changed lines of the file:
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@@
   (dnp no)
   (property "Reference" "U1703" (at 63.5 71.12 0) (effects (font (size 1.27 1.27))))
-  (property "Value" "TPS56637RPAR VSYS to USB_PORT_5V 5.21V" (at 63.5 76.2 0) (effects (font (size 1.27 1.27))))
+  (property "Value" "TPS56637RPAR VSYS to USB_PORT_5V 5.06V nominal" (at 63.5 76.2 0) (effects (font (size 1.27 1.27))))
   (property "Footprint" "ducktop2:Texas_RPA0010A_VQFN-HR-10_3x3mm" (at 63.5 73.66 0) (effects (font (size 1.27 1.27)) (hide yes)))
   (property "Datasheet" "" (at 63.5 73.66 0) (effects (font (size 1.27 1.27)) (hide yes)))
